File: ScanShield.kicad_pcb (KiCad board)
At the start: 2 copper layers, 59 x 98 mm, 26 parts, among them J1 Barrel_Jack_Switch_Pin3Ring, J2 Ringlight, J3 Rotor, J4 Turntable, J5 Cam, J6 Conn_02x20_Odd_Even, J7 Conn_01x15, Q1 IRLZ34N, Q2 IRLZ34N, SW1 SW_SPDT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

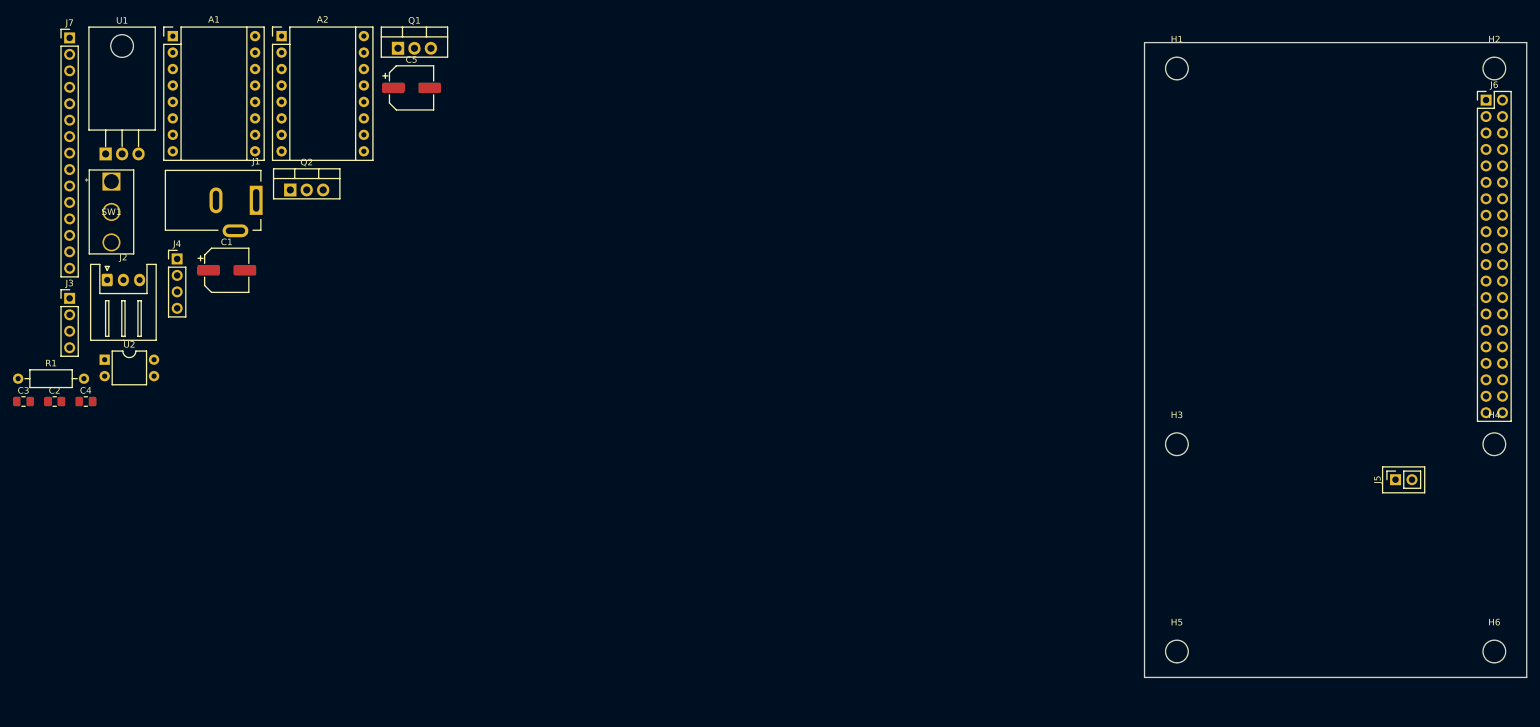
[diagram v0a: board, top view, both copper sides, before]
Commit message: Modified pcb, first variant
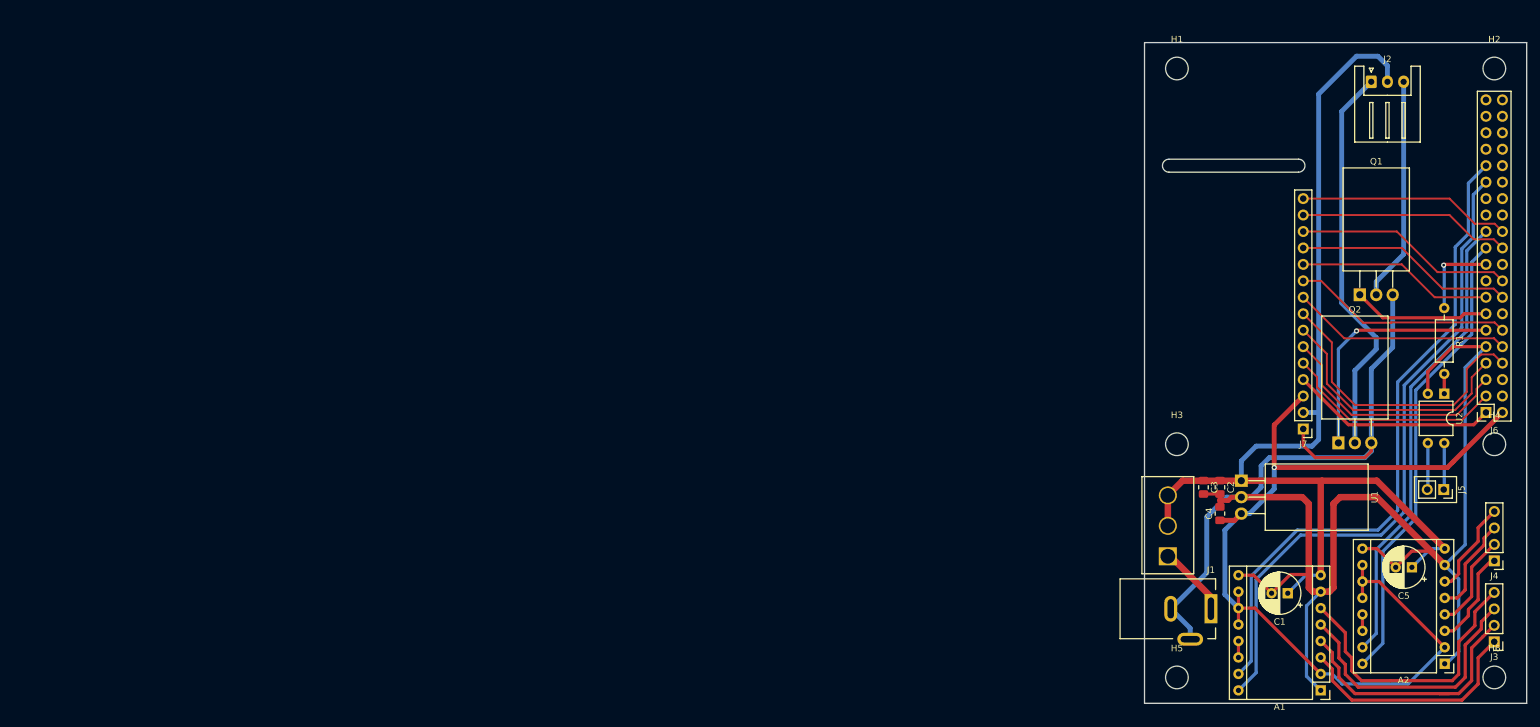
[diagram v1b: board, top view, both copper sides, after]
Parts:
- C1, C5: footprint Capacitor_SMD:CP_Elec_6.3x5.4 -> Capacitor_THT:CP_Radial_D6.3mm_P2.50mm
- C3: value 0.33u -> 10u
- J6: footprint Connector_PinHeader_2.54mm:PinHeader_2x20_P2.54mm_Vertical -> Connector_PinSocket_2.54mm:PinSocket_2x20_P2.54mm_Vertical
- Q1, Q2: footprint Package_TO_SOT_THT:TO-220-3_Vertical -> Package_TO_SOT_THT:TO-220-3_Horizontal_TabDown
- SW1: moved to B.Cu
- moved J3 226.2 mm to (99.0, 128.5), turned to 180 degrees
- moved R1 220.4 mm to (91.3, 77.0), turned to -90 degrees
- moved J4 208.6 mm to (99.0, 116.0), turned to 180 degrees
- moved U2 206.9 mm to (91.3, 90.2), turned to -90 degrees
- moved A2 204.0 mm to (91.3, 131.9), turned to 180 degrees
- moved A1 204.0 mm to (72.2, 136.0), turned to 180 degrees
- moved J7 199.8 mm to (69.5, 95.6), turned to 180 degrees
- moved J2 197.5 mm to (80.0, 42.0)
- moved C3 182.6 mm to (54.1, 104.6), turned to -90 degrees
- moved U1 182.4 mm to (59.9, 103.6), turned to -90 degrees
- moved C2 180.4 mm to (56.6, 104.6), turned to -90 degrees
- moved C4 175.9 mm to (56.6, 108.7), turned to 90 degrees
- moved SW1 173.0 mm to (48.6, 115.3)
- moved C5 171.2 mm to (86.3, 117.0), turned to 180 degrees
- moved C1 171.2 mm to (67.1, 121.0), turned to 180 degrees
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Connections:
- net Turntable_Dir renamed GPIO9
- net Turntable_Step renamed GPIO11
- C2 pad 1: GND -> VMOT
- C2 pad 2: VMOT -> GND
- Q1 pad 1: GPIO17 -> GPIO27
- Q2 pad 1: GPIO27 -> GPIO17
- SW1 pad 1: unconnected-(SW1-Pad1) -> Net-(J1-Pad1)
- SW1 pad 2: Net-(J1-Pad1) -> VMOT
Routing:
- net GND: track 0.00 -> 276.6 mm
- net VMOT: track 0.00 -> 168.1 mm
- net +5V: track 0.00 -> 147.9 mm, vias 0 -> 1
- net GPIO5: track 0.00 -> 101.6 mm
- net GPIO6: track 0.00 -> 101.6 mm
- net GPIO11: track 0.00 -> 72.1 mm
- net GPIO9: track 0.00 -> 72.1 mm
- net Net-(J2-Pad1): track 0.00 -> 61.2 mm
- net GPIO14: track 0.00 -> 46.0 mm
- net Net-(A1-Pad6): track 0.00 -> 44.1 mm
- net Net-(A1-Pad5): track 0.00 -> 41.6 mm
- net Net-(A1-Pad4): track 0.00 -> 40.6 mm
- net GPIO4: track 0.00 -> 40.4 mm
- net GPIO17: track 0.00 -> 38.5 mm, vias 0 -> 1
- net GPIO3: track 0.00 -> 37.2 mm
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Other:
- board size 59 x 98 mm -> 59 x 102 mm

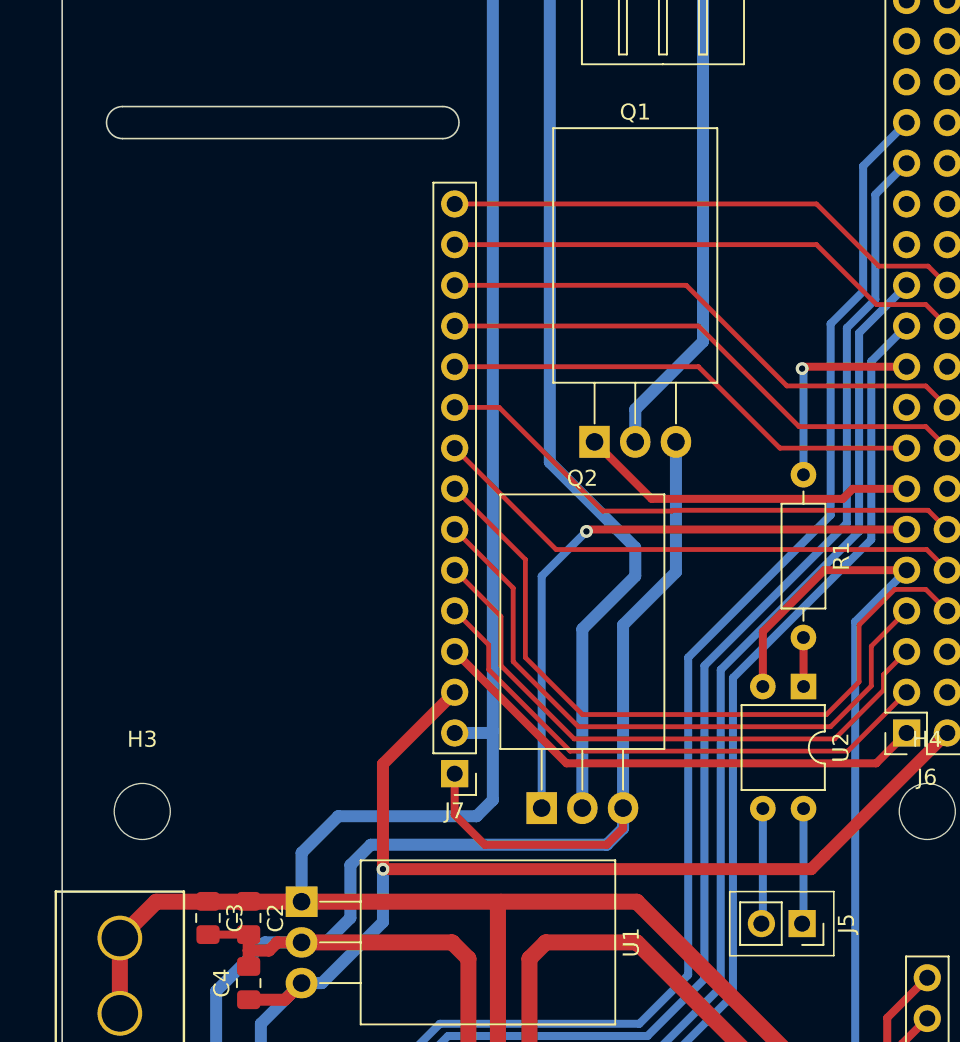
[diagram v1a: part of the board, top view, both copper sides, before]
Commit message: Changed board cutout
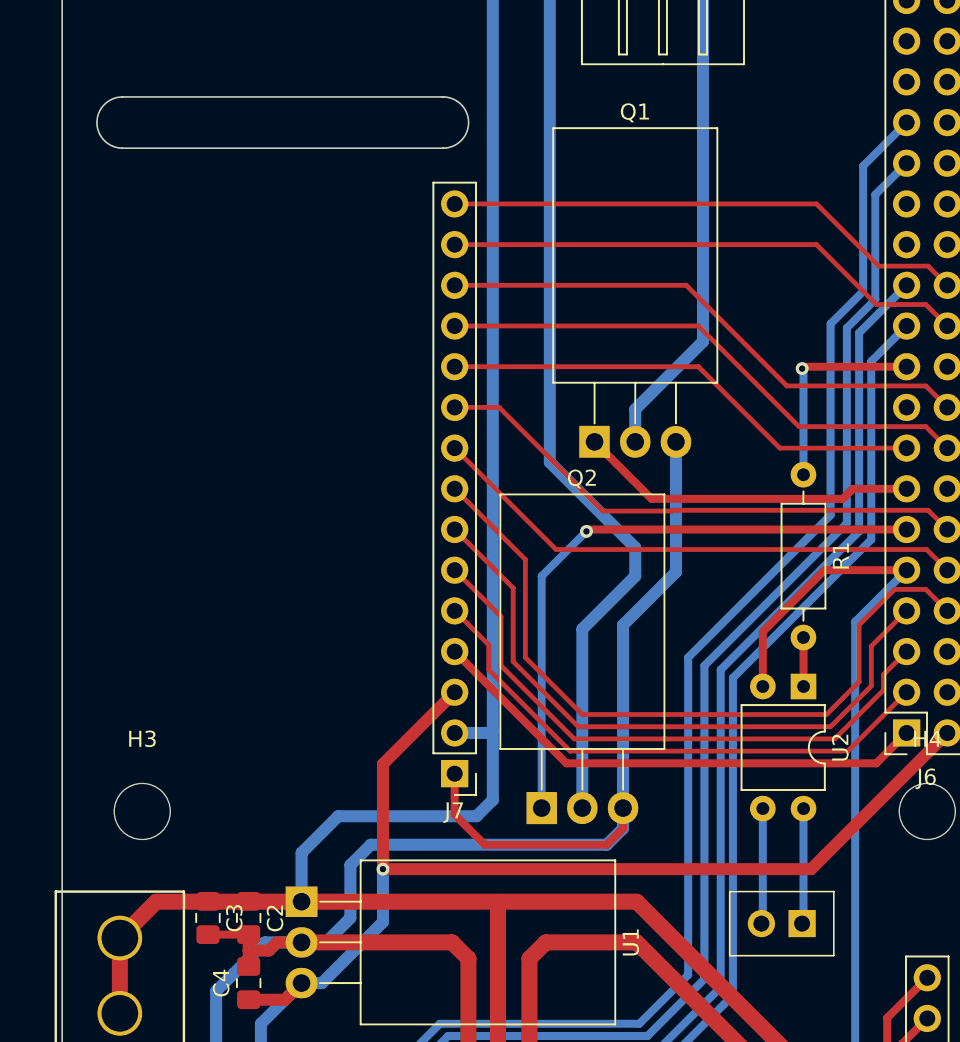
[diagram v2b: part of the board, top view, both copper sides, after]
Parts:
- J5: moved to B.Cu
- turned J5 to 90 degrees
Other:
- outline, holes or cut-outs redrawn
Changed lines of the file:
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@@
-    )
-  )
-  (footprint "Connector_PinSocket_2.54mm:PinSocket_1x02_P2.54mm_Vertical" locked (layer "F.Cu")
-    (at 91.186 105 -90)
-    (descr "Through hole straight socket strip, 1x02, 2.54mm pitch, single row (from Kicad 4.0.7), script generated")
-    (tags "Through hole socket strip THT 1x02 2.54mm single row")
-    (property "Sheetfile" "ScanShield.kicad_sch")
-    (property "Sheetname" "")
-    (attr through_hole)
-    (fp_text reference "J5" (at 0 -2.77 90) (layer "F.SilkS")
-      (effects (font (size 1 1) (thickness 0.15)))
-    )
-    (fp_text value "Cam" (at 0 5.31 90) (layer "F.Fab")
-      (effects (font (size 1 1) (thickness 0.15)))
-    )
-    (fp_text user "${REFERENCE}" (at 0 1.27) (layer "F.Fab")
-      (effects (font (size 1 1) (thickness 0.15)))
-    )
-    (fp_line (start -1.33 1.27) (end -1.33 3.87) (layer "F.SilkS") (width 0.12))
-    (fp_line (start 1.33 1.27) (end 1.33 3.87) (layer "F.SilkS") (width 0.12))
-    (fp_line (start 1.33 -1.33) (end 1.33 0) (layer "F.SilkS") (width 0.12))
-    (fp_line (start -1.33 1.27) (end 1.33 1.27) (layer "F.SilkS") (width 0.12))
-    (fp_line (start 0 -1.33) (end 1.33 -1.33) (layer "F.SilkS") (width 0.12))
-    (fp_line (start -1.33 3.87) (end 1.33 3.87) (layer "F.SilkS") (width 0.12))
-    (fp_line (start 1.75 -1.8) (end 1.75 4.3) (layer "F.CrtYd") (width 0.05))
-    (fp_line (start -1.8 -1.8) (end 1.75 -1.8) (layer "F.CrtYd") (width 0.05))
-    (fp_line (start -1.8 4.3) (end -1.8 -1.8) (layer "F.CrtYd") (width 0.05))
-    (fp_line (start 1.75 4.3) (end -1.8 4.3) (layer "F.CrtYd") (width 0.05))
-    (fp_line (start -1.27 -1.27) (end 0.635 -1.27) (layer "F.Fab") (width 0.1))
-    (fp_line (start 0.635 -1.27) (end 1.27 -0.635) (layer "F.Fab") (width 0.1))
-    (fp_line (start 1.27 -0.635) (end 1.27 3.81) (layer "F.Fab") (width 0.1))
-    (fp_line (start -1.27 3.81) (end -1.27 -1.27) (layer "F.Fab") (width 0.1))
-    (fp_line (start 1.27 3.81) (end -1.27 3.81) (layer "F.Fab") (width 0.1))
-    (pad "1" thru_hole rect locked (at 0 0 270) (size 1.7 1.7) (drill 1) (layers *.Cu *.Mask)
-      (net 19 "Net-(J5-Pad1)") (pinfunction "Pin_1") (pintype "passive"))
-    (pad "2" thru_hole oval locked (at 0 2.54 270) (size 1.7 1.7) (drill 1) (layers *.Cu *.Mask)
-      (net 20 "Net-(J5-Pad2)") (pinfunction "Pin_2") (pintype "passive"))
-    (model "${KICAD6_3DMODEL_DIR}/Connector_PinSocket_2.54mm.3dshapes/PinSocket_1x02_P2.54mm_Vertical.wrl"
-      (offset (xyz 0 0 0))
-      (scale (xyz 1 1 1))
-      (rotate (xyz 0 0 0))
     )
   )
@@
     (pad "3" thru_hole oval (at -3.2 4.7 90) (size 2 4) (drill oval 1 3) (layers *.Cu *.Mask)
       (net 1 "GND") (pintype "passive"))
-    (model "${KICAD6_3DMODEL_DIR}/Connector_BarrelJack.3dshapes/BarrelJack_Kycon_KLDX-0202-xC_Horizontal.wrl"
-      (offset (xyz 0 0 0))
-      (scale (xyz 1 1 1))
-      (rotate (xyz 0 0 0))
+    (model "${KIPRJMOD}/Library/KLDX-0202-A.stp"
+      (offset (xyz -14 0 5.25))
+      (scale (xyz 1 1 1))
+      (rotate (xyz -90 0 90))
     )
   )
@@
     (pad "3" thru_hole circle (at 0 -9.398) (size 2.794 2.794) (drill 2.286) (layers *.Cu *.Mask)
       (net 7 "VMOT") (pinfunction "C") (pintype "passive"))
+    (model "${KIPRJMOD}/Library/1101M2S3CQE2.stp"
+      (offset (xyz 0 -4.75 0))
+      (scale (xyz 1 1 1))
+      (rotate (xyz 0 0 90))
+    )
+  )
+  (footprint "Connector_PinSocket_2.54mm:PinSocket_1x02_P2.54mm_Vertical" (layer "B.Cu")
+    (at 91.186 105 90)
+    (descr "Through hole straight socket strip, 1x02, 2.54mm pitch, single row (from Kicad 4.0.7), script generated")
+    (tags "Through hole socket strip THT 1x02 2.54mm single row")
+    (property "Sheetfile" "ScanShield.kicad_sch")
+    (property "Sheetname" "")
+    (attr through_hole)
+    (fp_text reference "J5" (at 0 2.77 90) (layer "B.SilkS")
+      (effects (font (size 1 1) (thickness 0.15)) (justify mirror))
+    )
+    (fp_text value "Cam" (at 0 -5.31 90) (layer "B.Fab")
+      (effects (font (size 1 1) (thickness 0.15)) (justify mirror))
+    )
+    (fp_text user "${REFERENCE}" (at 0 -1.27) (layer "B.Fab")
+      (effects (font (size 1 1) (thickness 0.15)) (justify mirror))
+    )
+    (fp_line (start -1.33 -1.27) (end -1.33 -3.87) (layer "B.SilkS") (width 0.12))
+    (fp_line (start 1.33 -1.27) (end 1.33 -3.87) (layer "B.SilkS") (width 0.12))
+    (fp_line (start 1.33 1.33) (end 1.33 0) (layer "B.SilkS") (width 0.12))
+    (fp_line (start -1.33 -1.27) (end 1.33 -1.27) (layer "B.SilkS") (width 0.12))
+    (fp_line (start 0 1.33) (end 1.33 1.33) (layer "B.SilkS") (width 0.12))
+    (fp_line (start -1.33 -3.87) (end 1.33 -3.87) (layer "B.SilkS") (width 0.12))
+    (fp_line (start 1.75 1.8) (end 1.75 -4.3) (layer "B.CrtYd") (width 0.05))
+    (fp_line (start -1.8 1.8) (end 1.75 1.8) (layer "B.CrtYd") (width 0.05))
+    (fp_line (start -1.8 -4.3) (end -1.8 1.8) (layer "B.CrtYd") (width 0.05))
+    (fp_line (start 1.75 -4.3) (end -1.8 -4.3) (layer "B.CrtYd") (width 0.05))
+    (fp_line (start -1.27 1.27) (end 0.635 1.27) (layer "B.Fab") (width 0.1))
+    (fp_line (start 0.635 1.27) (end 1.27 0.635) (layer "B.Fab") (width 0.1))
+    (fp_line (start 1.27 0.635) (end 1.27 -3.81) (layer "B.Fab") (width 0.1))
+    (fp_line (start -1.27 -3.81) (end -1.27 1.27) (layer "B.Fab") (width 0.1))
+    (fp_line (start 1.27 -3.81) (end -1.27 -3.81) (layer "B.Fab") (width 0.1))
+    (pad "1" thru_hole rect locked (at 0 0 90) (size 1.7 1.7) (drill 1) (layers *.Cu *.Mask)
+      (net 19 "Net-(J5-Pad1)") (pinfunction "Pin_1") (pintype "passive"))
+    (pad "2" thru_hole oval locked (at 0 -2.54 90) (size 1.7 1.7) (drill 1) (layers *.Cu *.Mask)
+      (net 20 "Net-(J5-Pad2)") (pinfunction "Pin_2") (pintype "passive"))
+    (model "${KICAD6_3DMODEL_DIR}/Connector_PinSocket_2.54mm.3dshapes/PinSocket_1x02_P2.54mm_Vertical.wrl"
+      (offset (xyz 0 0 0))
+      (scale (xyz 1 1 1))
+      (rotate (xyz 0 0 0))
+    )
   )
   (gr_line locked (start 86.666 103) (end 86.666 107) (layer "F.SilkS") (width 0.1))
@@
   (gr_line (start 44.6 103) (end 52.6 103) (layer "F.SilkS") (width 0.15))
   (gr_line locked (start 93.166 103) (end 86.666 103) (layer "F.SilkS") (width 0.1))
-  (gr_line (start 48.77 56) (end 68.77 56) (layer "Edge.Cuts") (width 0.1))
   (gr_line (start 104 138) (end 45 138) (layer "Edge.Cuts") (width 0.1))
+  (gr_arc (start 68.77 53.4) (mid 70.37 55) (end 68.77 56.6) (layer "Edge.Cuts") (width 0.1))
   (gr_line (start 45 138) (end 45 36) (layer "Edge.Cuts") (width 0.1))
-  (gr_arc (start 48.77 56) (mid 47.77 55) (end 48.77 54) (layer "Edge.Cuts") (width 0.1))
   (gr_line (start 104 36) (end 104 138) (layer "Edge.Cuts") (width 0.1))
-  (gr_arc (start 68.77 54) (mid 69.77 55) (end 68.77 56) (layer "Edge.Cuts") (width 0.1))
+  (gr_line (start 48.77 53.4) (end 68.77 53.4) (layer "Edge.Cuts") (width 0.1))
+  (gr_line (start 68.77 56.6) (end 48.77 56.6) (layer "Edge.Cuts") (width 0.1))
+  (gr_arc (start 48.77 56.6) (mid 47.17 55) (end 48.77 53.4) (layer "Edge.Cuts") (width 0.1))
   (gr_line (start 45 36) (end 104 36) (layer "Edge.Cuts") (width 0.1))
-  (gr_line (start 48.77 54) (end 68.77 54) (layer "Edge.Cuts") (width 0.1))
   (segment (start 92.574 82.94) (end 97.71 82.94) (width 0.5) (layer "F.Cu") (net 1))
   (segment (start 70.976 120.76) (end 72.2 120.76) (width 1) (layer "F.Cu") (net 1))

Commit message: Second pcb draft
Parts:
- removed C2: 0.33u, Capacitor_SMD:C_0805_2012Metric_Pad1.18x1.45mm_HandSolder
- J7: moved to B.Cu
- Q1, Q2: footprint Package_TO_SOT_THT:TO-220-3_Horizontal_TabDown -> Package_TO_SOT_THT:TO-220-3_Vertical
- U1: footprint Package_TO_SOT_THT:TO-220-3_Horizontal_TabDown -> Connector_PinHeader_2.54mm:PinHeader_1x03_P2.54mm_Vertical
- moved J2 4.58 mm to (84.4, 40.8)
- moved C4 3.42 mm to (54.1, 111.0)
- moved U1 3.23 mm to (57.7, 105.9), turned to 0 degrees
- moved C3 2.29 mm to (54.1, 106.9)
- moved A2 0.86 mm to (92.2, 131.9)
- moved C5 0.86 mm to (87.1, 117.0)
- moved A1 0.70 mm to (72.9, 136.0)
- moved C1 0.70 mm to (67.8, 121.0)
- moved SW1 0.10 mm to (48.7, 115.3)
- turned J7 to 0 degrees
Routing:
- net GND: track 276.6 -> 270.7 mm
- net Net-(J2-Pad1): track 61.2 -> 66.1 mm
- net VMOT: track 168.1 -> 172.8 mm
- net GPIO14: track 46.0 -> 42.7 mm
- net Net-(J2-Pad3): track 34.6 -> 37.7 mm
- net GPIO4: track 40.4 -> 38.0 mm
- net GPIO2: track 34.3 -> 36.4 mm
- net GPIO3: track 37.2 -> 35.7 mm
- net Net-(A2-Pad5): track 15.1 -> 13.6 mm
- net Net-(A2-Pad4): track 14.8 -> 13.6 mm
- net Net-(A2-Pad6): track 14.6 -> 13.6 mm
- net Net-(A2-Pad3): track 15.1 -> 14.3 mm
- net GPIO18: track 33.9 -> 34.6 mm
- net Net-(A1-Pad6): track 44.1 -> 43.5 mm
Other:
- board text added: "+"
- board text added: "-"
- board text added: "12V"
- board text added: "3.3V"
- board text added: "5V"
- board text added: "CAM"
- board text added: "GND"
- board text added: "GPIO14"
- board text added: "GPIO15"
- board text added: "GPIO18"
- board text added: "GPIO2"
- board text added: "GPIO22"
- board text added: "GPIO23"
- board text added: "GPIO24"
- board text added: "GPIO25"
- board text added: "GPIO3"
- board text added: "GPIO4"
- board text added: "GPIO8"
